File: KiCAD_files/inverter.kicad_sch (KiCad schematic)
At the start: 10 parts, among them J101 Harting-15 and Wago 6

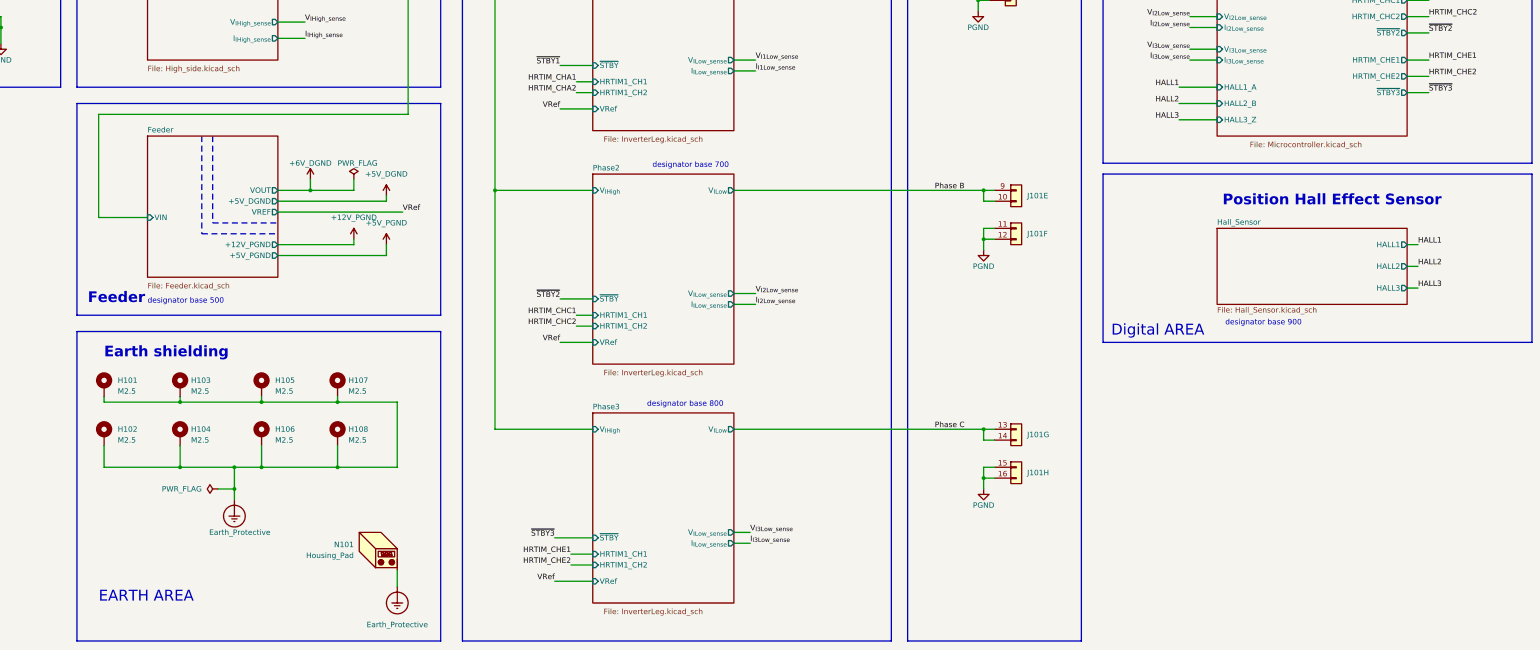
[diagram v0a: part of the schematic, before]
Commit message: Added ERC rules for galvanic isolation. Modified SPIN pinout.
Signed-off-by: Jean Alinei <jean.alinei@laas.fr>
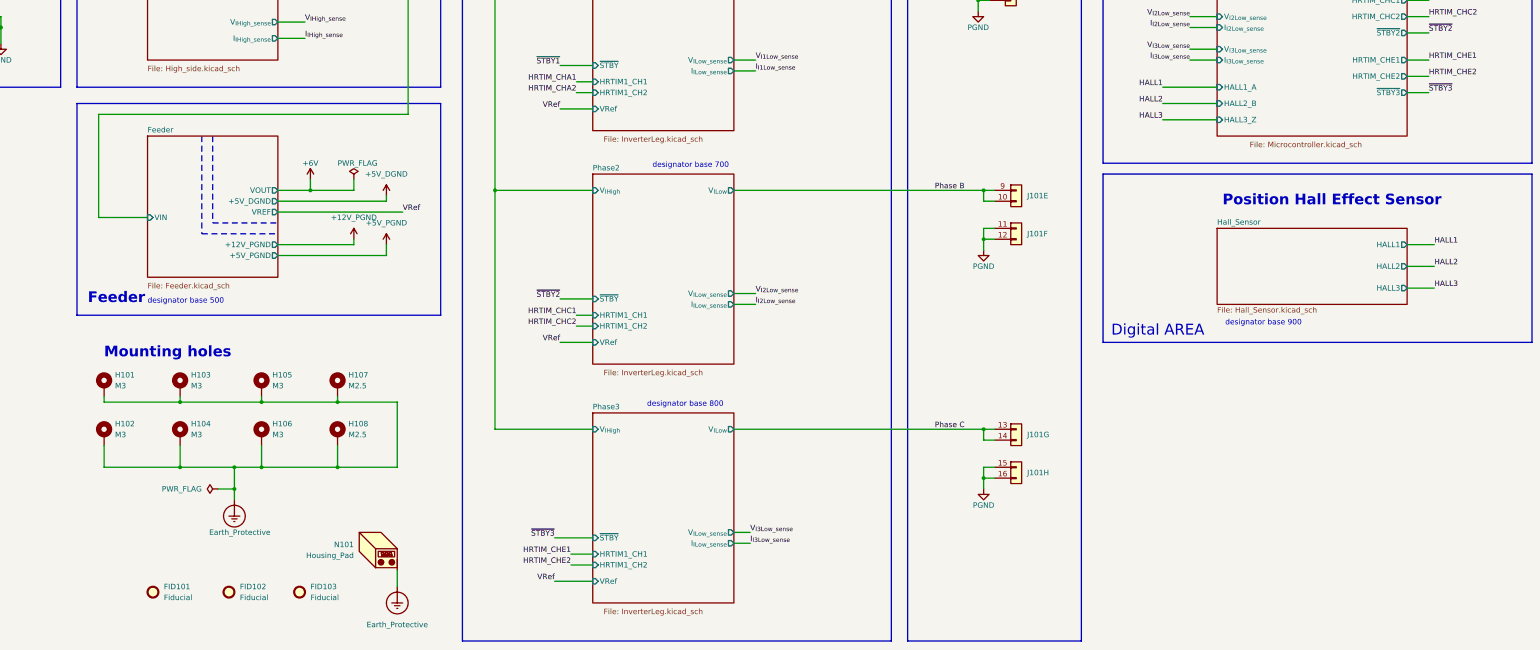
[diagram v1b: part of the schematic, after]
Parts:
- added FID101, FID102, FID103: Fiducial, Fiducial:Fiducial_0.75mm_Mask1.5mm, symbol Mechanical:Fiducial
- H101, H102, H103, H104, H105, H106: value M2.5 -> M3; footprint MountingHole:MountingHole_2.7mm_M2.5_DIN965_Pad_TopOnly -> MountingHole:MountingHole_3.2mm_M3_DIN965_Pad_TopOnly
- H108: footprint MountingHole:MountingHole_2.7mm_M2.5_DIN965_Pad_TopOnly -> MountingHole:MountingHole_2.7mm_M2.5_ISO7380_Pad_TopOnly
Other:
- note added: "Mounting holes"
- note removed: "EARTH AREA"
- note removed: "Earth shielding"
